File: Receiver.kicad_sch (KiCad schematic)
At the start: 21 parts, among them J15 ReceiverRS485, J23 ReceiverData, U17 AMS1117-5.0, U23 MAX485EE

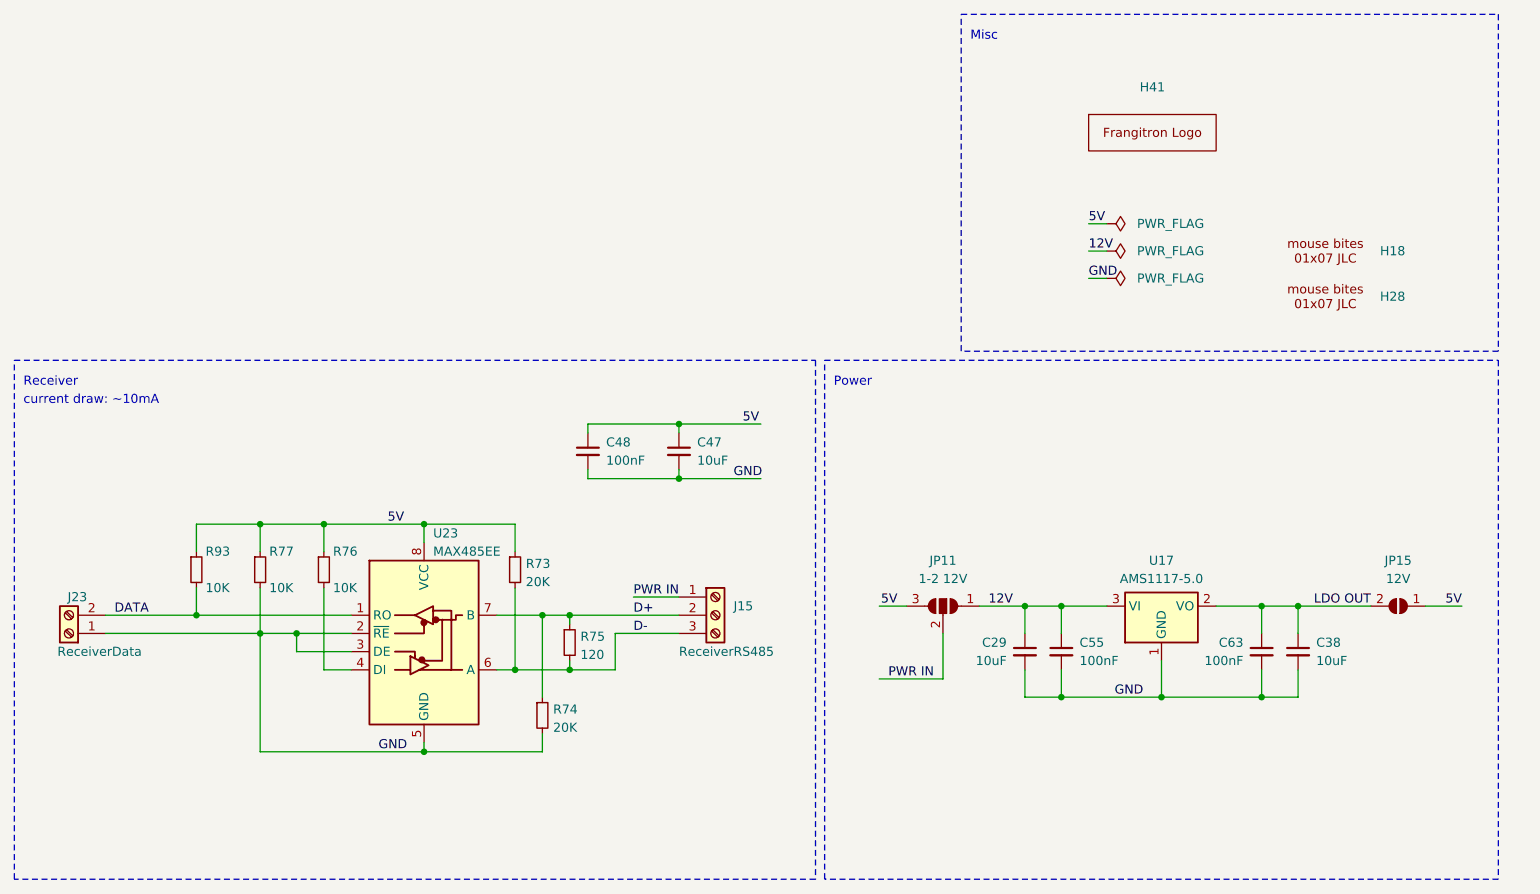
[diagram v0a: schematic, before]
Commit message: rename to v1 (to match silkscreen), improve readme and schematics layouts
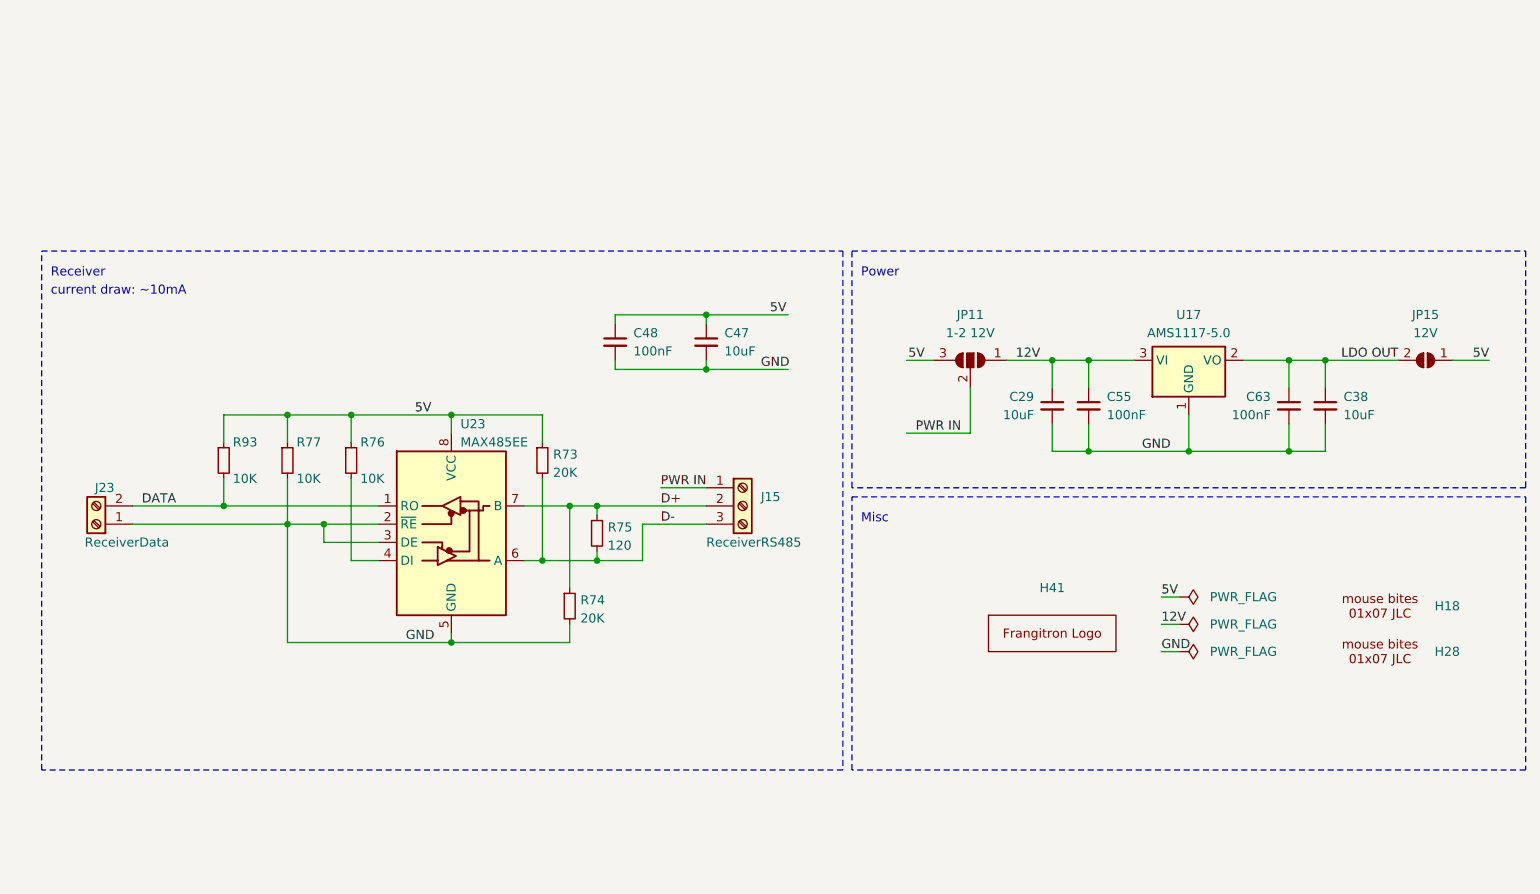
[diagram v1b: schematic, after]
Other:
- moved on the sheet: C29, C38, C47, C48, C55, C63, H18, H28, H41, J15, J23, JP11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
